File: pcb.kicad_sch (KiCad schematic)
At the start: 49 parts, among them J1 USB_B_Mini, J2 Conn_ARM_JTAG_SWD_20, J3 Micro_SD_Card_Det1, SW1 SW_RESET, U1 STM32H750VBTx, U2 USBLC6-2P6, U3 TLV1117-33, U4 W25Q128JVS, Y1 8MHz

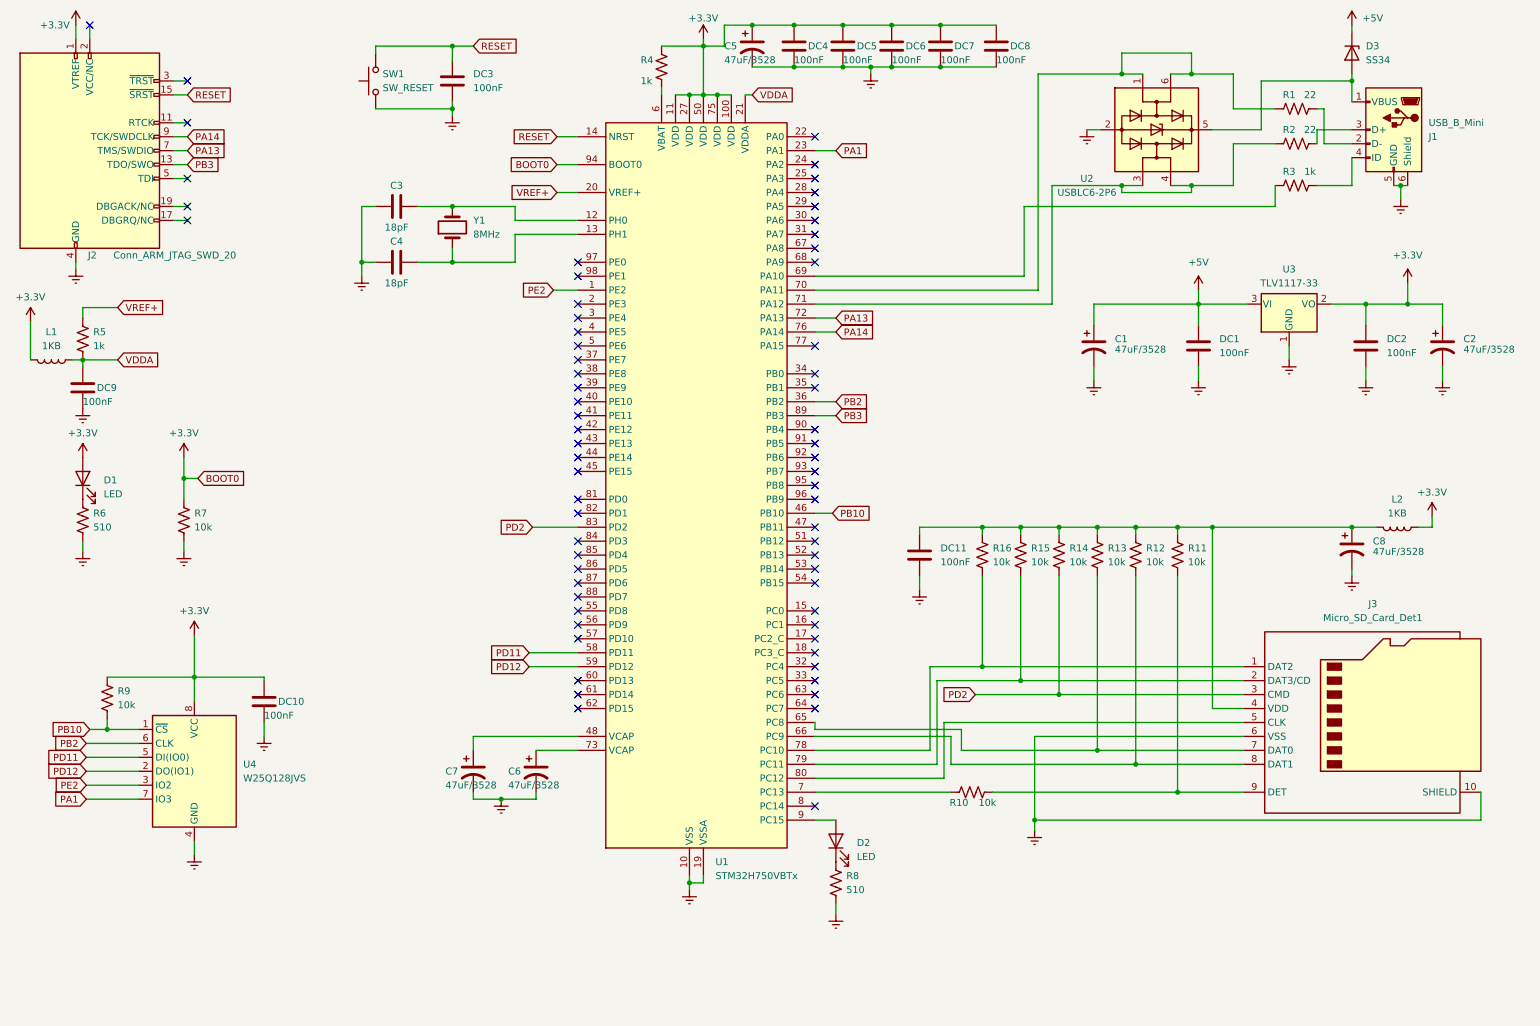
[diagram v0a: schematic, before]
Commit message: SCH: Schematic mostly finished, missing pin connectors
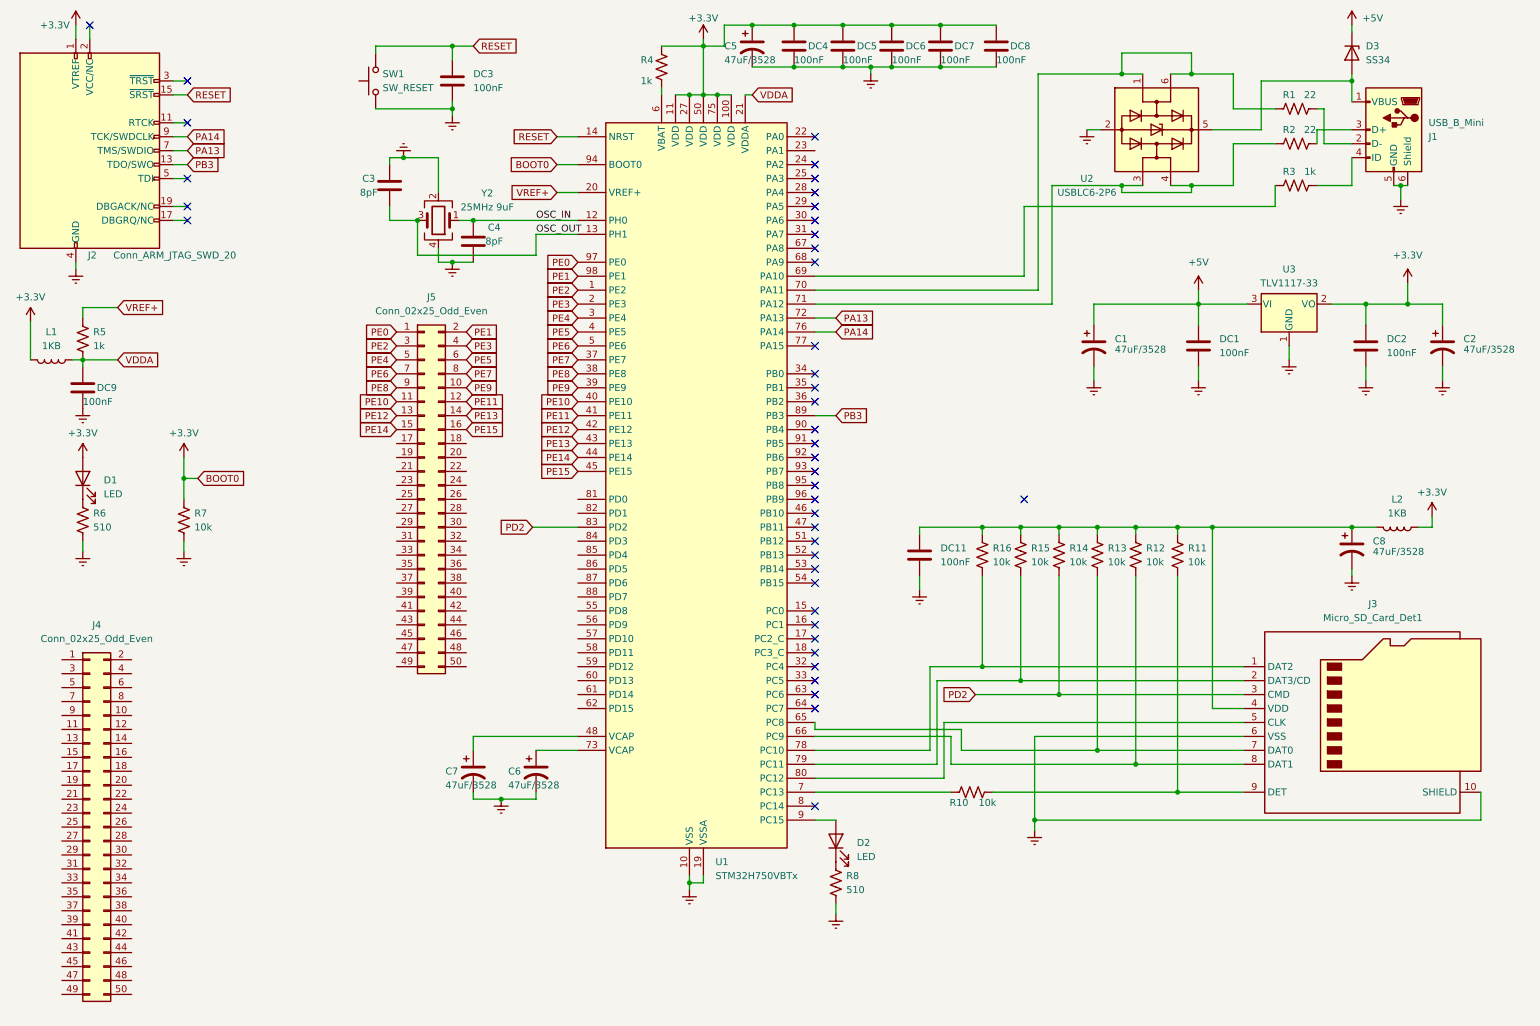
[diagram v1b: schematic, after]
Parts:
- removed DC10: 100nF, symbol Device:C
- removed R9: 10k, symbol Device:R_US
- removed U4: W25Q128JVS, Package_SO:SOIC-8_5.23x5.23mm_P1.27mm, symbol Memory_Flash:W25Q128JVS
- removed Y1: 8MHz, symbol Device:Crystal
- added J4, J5: Conn_02x25_Odd_Even, Connector_PinSocket_2.54mm:PinSocket_2x25_P2.54mm_Vertical, symbol Connector_Generic:Conn_02x25_Odd_Even
- added Y2: 25MHz 9uF, Crystal:Crystal_SMD_2016-4Pin_2.0x1.6mm, symbol Device:Crystal_GND23
- C1, C2, C5, C6, C7, C8: footprint (none) -> Capacitor_SMD:C_1206_3216Metric
- C3, C4: value 18pF -> 8pF; footprint (none) -> Capacitor_SMD:C_0402_1005Metric
- D1, D2: footprint (none) -> LED_SMD:LED_0603_1608Metric
- DC1, DC11, DC2, DC3, DC4, DC5, DC6, DC7, DC8, DC9: footprint (none) -> Capacitor_SMD:C_0402_1005Metric
- J1: footprint (none) -> Connector_USB:USB_Mini-B_Wuerth_65100516121_Horizontal
- J2: footprint (none) -> Connector_TE-Connectivity:TE_MATE-N-LOK_1-794070-x_2x10_P4.14mm_Vertical
- J3: footprint (none) -> Connector_Card:microSD_HC_Molex_104031-0811
- L1, L2: footprint (none) -> Inductor_SMD:L_0402_1005Metric
- R1, R10, R11, R12, R13, R14, R15, R16, R2, R7: footprint (none) -> Resistor_SMD:R_0402_1005Metric
- R3, R4, R5, R6, R8: footprint (none) -> Resistor_SMD:R_0603_1608Metric
- SW1: footprint (none) -> Button_Switch_SMD:SW_SPST_CK_RS282G05A3
- U3: footprint (none) -> Package_TO_SOT_SMD:SOT-223
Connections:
- net Earth: now also C4.2, Y2.2, Y2.4; no longer C4.1
- net PE2: now also J5.3 (Pin_3)
- net OSC_OUT: now reaches U1.13 (PH1)
- net OSC_OUT: now also C3.2, Y2.3; no longer C4.2
- net OSC_IN: now reaches U1.12 (PH0)
- net OSC_IN: now also C4.1, Y2.1; no longer C3.2
- net PE3: now reaches U1.2 (PE3)
- net PE3: now also J5.4 (Pin_4)
- net PE4: now reaches U1.3 (PE4)
- net PE4: now also J5.5 (Pin_5)
- net PE7: now reaches U1.37 (PE7)
- net PE7: now also J5.8 (Pin_8)
- net PE8: now reaches U1.38 (PE8)
- net PE8: now also J5.9 (Pin_9)
- net PE9: now reaches U1.39 (PE9)
- net PE9: now also J5.10 (Pin_10)
- net PE5: now reaches U1.4 (PE5)
- net PE5: now also J5.6 (Pin_6)
- net PE10: now reaches U1.40 (PE10)
- net PE10: now also J5.11 (Pin_11)
- net PE11: now reaches U1.41 (PE11)
- net PE11: now also J5.12 (Pin_12)
- net PE12: now reaches U1.42 (PE12)
- net PE12: now also J5.13 (Pin_13)
- net PE13: now reaches U1.43 (PE13)
- net PE13: now also J5.14 (Pin_14)
- net PE14: now reaches U1.44 (PE14)
- net PE14: now also J5.15 (Pin_15)
- net PE15: now reaches U1.45 (PE15)
- net PE15: now also J5.16 (Pin_16)
- net PE6: now reaches U1.5 (PE6)
- net PE6: now also J5.7 (Pin_7)
- net PE0: now reaches U1.97 (PE0)
- net PE0: now also J5.1 (Pin_1)
- net PE1: now reaches U1.98 (PE1)
- net PE1: now also J5.2 (Pin_2)
- net PA1: no longer names the net of U1.23 (PA1)
- net PB10: no longer names the net of U1.46 (PB10)
- net PB2: no longer names the net of U1.36 (PB2)
- net PD11: no longer names the net of U1.58 (PD11)
- net PD12: no longer names the net of U1.59 (PD12)
- no-connect marks 66 -> 41
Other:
- moved on the sheet: C3, C4

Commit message: ROUTE: Routing finished, still needs to be re-worked but functionality is in place
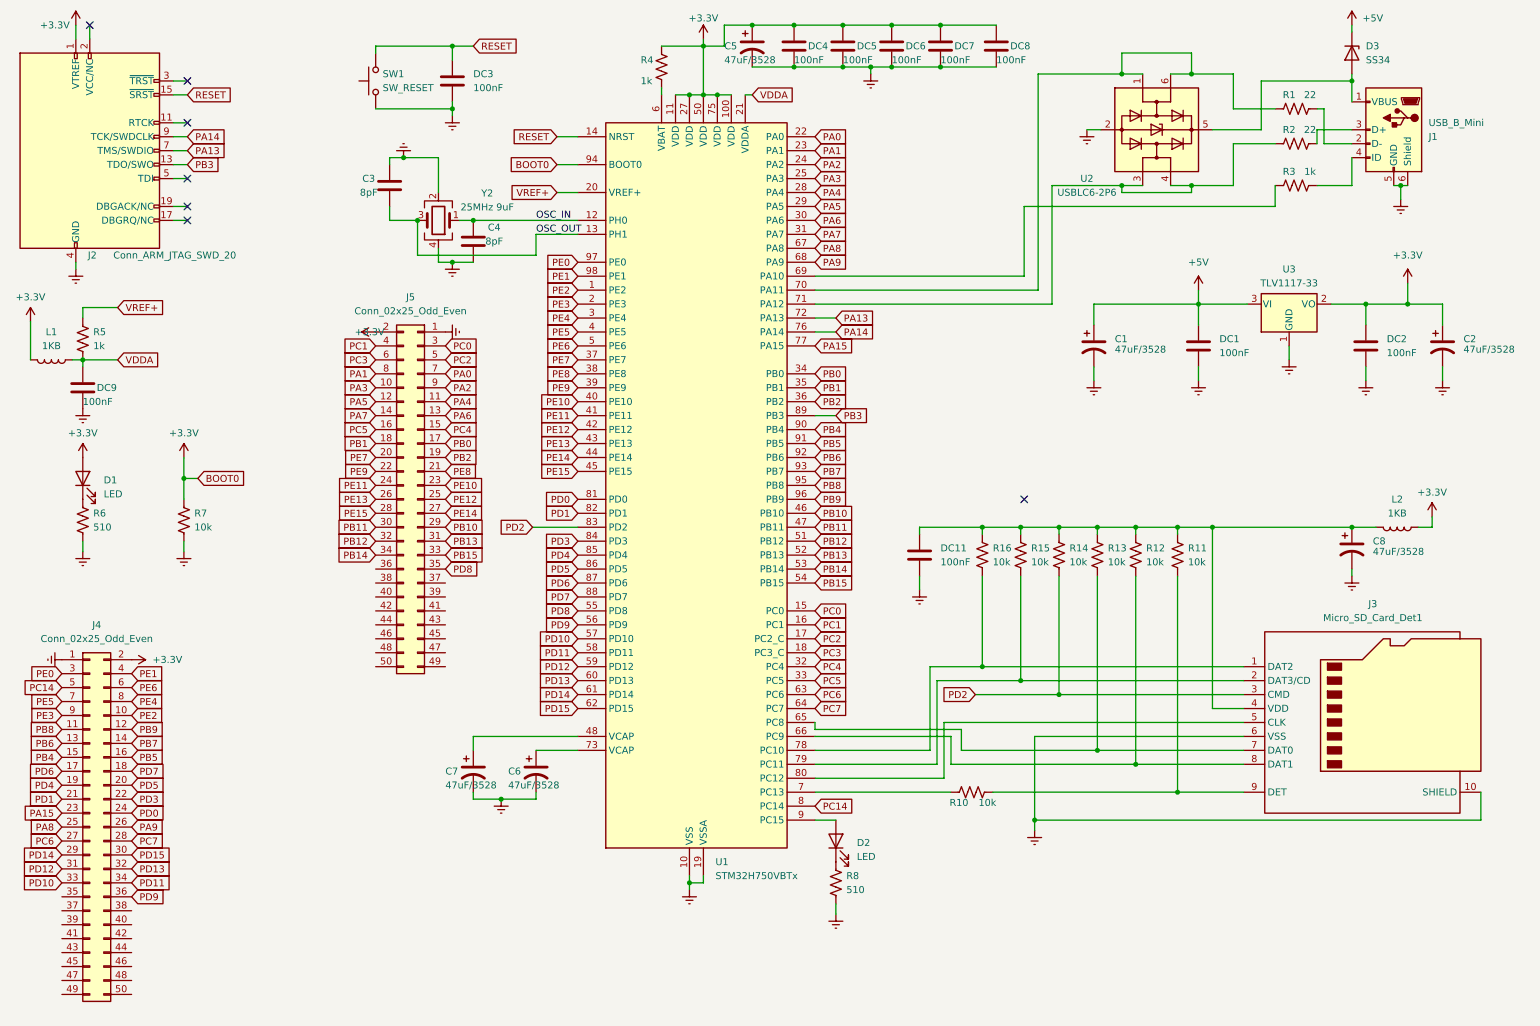
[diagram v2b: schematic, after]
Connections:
- net +3.3V: now also J4.2 (Pin_2), J5.2 (Pin_2)
- net Earth: now also J4.1 (Pin_1), J5.1 (Pin_1)
- net PE0: now also J4.3 (Pin_3); no longer J5.1 (Pin_1)
- net PE1: now also J4.4 (Pin_4); no longer J5.2 (Pin_2)
- net PE10: now also J5.23 (Pin_23); no longer J5.11 (Pin_11)
- net PE11: now also J5.24 (Pin_24); no longer J5.12 (Pin_12)
- net PE12: now also J5.25 (Pin_25); no longer J5.13 (Pin_13)
- net PE13: now also J5.26 (Pin_26); no longer J5.14 (Pin_14)
- net PE14: now also J5.27 (Pin_27); no longer J5.15 (Pin_15)
- net PE15: now also J5.28 (Pin_28); no longer J5.16 (Pin_16)
- net PE2: now also J4.10 (Pin_10); no longer J5.3 (Pin_3)
- net PE3: now also J4.9 (Pin_9); no longer J5.4 (Pin_4)
- net PE4: now also J4.8 (Pin_8); no longer J5.5 (Pin_5)
- net PE5: now also J4.7 (Pin_7); no longer J5.6 (Pin_6)
- net PE6: now also J4.6 (Pin_6); no longer J5.7 (Pin_7)
- net PE7: now also J5.20 (Pin_20); no longer J5.8 (Pin_8)
- net PE8: now also J5.21 (Pin_21); no longer J5.9 (Pin_9)
- net PE9: now also J5.22 (Pin_22); no longer J5.10 (Pin_10)
- net PB8: now reaches J4.11 (Pin_11)
- net PB8: now also U1.95 (PB8)
- net PB9: now reaches J4.12 (Pin_12)
- net PB9: now also U1.96 (PB9)
- net PB6: now reaches J4.13 (Pin_13)
- net PB6: now also U1.92 (PB6)
- net PB7: now reaches J4.14 (Pin_14)
- net PB7: now also U1.93 (PB7)
- net PB4: now reaches J4.15 (Pin_15)
- net PB4: now also U1.90 (PB4)
- net PB5: now reaches J4.16 (Pin_16)
- net PB5: now also U1.91 (PB5)
- net PD6: now reaches J4.17 (Pin_17)
- net PD6: now also U1.87 (PD6)
- net PD7: now reaches J4.18 (Pin_18)
- net PD7: now also U1.88 (PD7)
- net PD4: now reaches J4.19 (Pin_19)
- net PD4: now also U1.85 (PD4)
- net PD5: now reaches J4.20 (Pin_20)
- net PD5: now also U1.86 (PD5)
- net PD1: now reaches J4.21 (Pin_21)
- net PD1: now also U1.82 (PD1)
- net PD3: now reaches J4.22 (Pin_22)
- net PD3: now also U1.84 (PD3)
- net PA15: now reaches J4.23 (Pin_23)
- net PA15: now also U1.77 (PA15)
- net PD0: now reaches J4.24 (Pin_24)
- net PD0: now also U1.81 (PD0)
- net PA8: now reaches J4.25 (Pin_25)
- net PA8: now also U1.67 (PA8)
- net PA9: now reaches J4.26 (Pin_26)
- net PA9: now also U1.68 (PA9)
- net PC6: now reaches J4.27 (Pin_27)
- net PC6: now also U1.63 (PC6)
- net PC7: now reaches J4.28 (Pin_28)
- net PC7: now also U1.64 (PC7)
- net PD14: now reaches J4.29 (Pin_29)
- net PD14: now also U1.61 (PD14)
- net PD15: now reaches J4.30 (Pin_30)
- net PD15: now also U1.62 (PD15)
- net PD12: now reaches J4.31 (Pin_31)
- net PD12: now also U1.59 (PD12)
- net PD13: now reaches J4.32 (Pin_32)
- net PD13: now also U1.60 (PD13)
- net PD10: now reaches J4.33 (Pin_33)
- net PD10: now also U1.57 (PD10)
- net PD11: now reaches J4.34 (Pin_34)
- net PD11: now also U1.58 (PD11)
- net PD9: now reaches J4.36 (Pin_36)
- net PD9: now also U1.56 (PD9)
- net PC14: now reaches J4.5 (Pin_5)
- net PC14: now also U1.8 (PC14)
- net PB0: now reaches J5.17 (Pin_17)
- net PB0: now also U1.34 (PB0)
- net PB1: now reaches J5.18 (Pin_18)
- net PB1: now also U1.35 (PB1)
- net PB2: now reaches J5.19 (Pin_19)
- net PB2: now also U1.36 (PB2)
- net PB10: now reaches J5.29 (Pin_29)
- net PB10: now also U1.46 (PB10)
- net PB11: now reaches J5.30 (Pin_30)
- net PB11: now also U1.47 (PB11)
- net PB13: now reaches J5.31 (Pin_31)
- net PB13: now also U1.52 (PB13)
- net PB12: now reaches J5.32 (Pin_32)
- net PB12: now also U1.51 (PB12)
- net PB15: now reaches J5.33 (Pin_33)
- net PB15: now also U1.54 (PB15)
- net PB14: now reaches J5.34 (Pin_34)
- net PB14: now also U1.53 (PB14)
- net PD8: now reaches J5.35 (Pin_35)
- net PD8: now also U1.55 (PD8)
- net PC0: now reaches U1.15 (PC0)
- net PC0: now also J5.3 (Pin_3)
- net PC1: now reaches U1.16 (PC1)
- net PC1: now also J5.4 (Pin_4)
- net PC2: now reaches U1.17 (PC2_C)
- net PC2: now also J5.5 (Pin_5)
- net PC3: now reaches U1.18 (PC3_C)
- net PC3: now also J5.6 (Pin_6)
- net PA0: now reaches U1.22 (PA0)
- net PA0: now also J5.7 (Pin_7)
- net PA1: now reaches U1.23 (PA1)
- net PA1: now also J5.8 (Pin_8)
- net PA2: now reaches U1.24 (PA2)
- net PA2: now also J5.9 (Pin_9)
- net PA3: now reaches U1.25 (PA3)
- net PA3: now also J5.10 (Pin_10)
- net PA4: now reaches U1.28 (PA4)
- net PA4: now also J5.11 (Pin_11)
- net PA5: now reaches U1.29 (PA5)
- net PA5: now also J5.12 (Pin_12)
- net PA6: now reaches U1.30 (PA6)
- net PA6: now also J5.13 (Pin_13)
- net PA7: now reaches U1.31 (PA7)
- net PA7: now also J5.14 (Pin_14)
- net PC4: now reaches U1.32 (PC4)
- net PC4: now also J5.15 (Pin_15)
- net PC5: now reaches U1.33 (PC5)
- net PC5: now also J5.16 (Pin_16)
- no-connect marks 41 -> 7
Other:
- moved on the sheet: J5

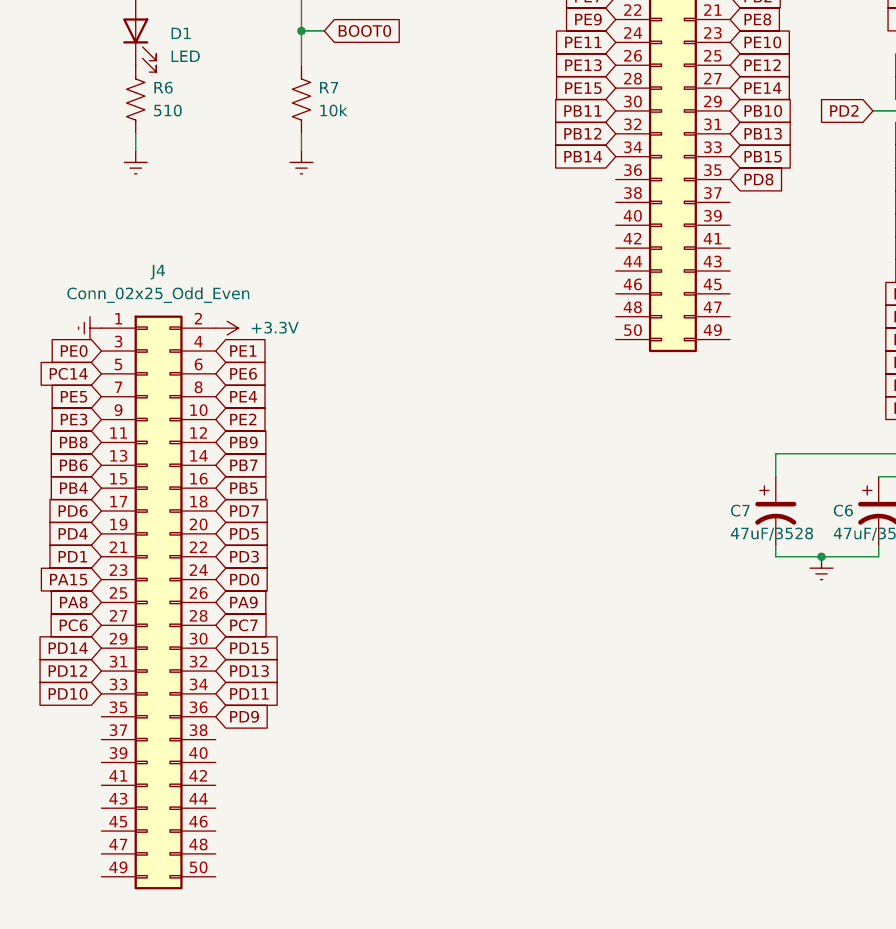
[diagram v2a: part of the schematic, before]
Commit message: PCB: Routing finished, first version
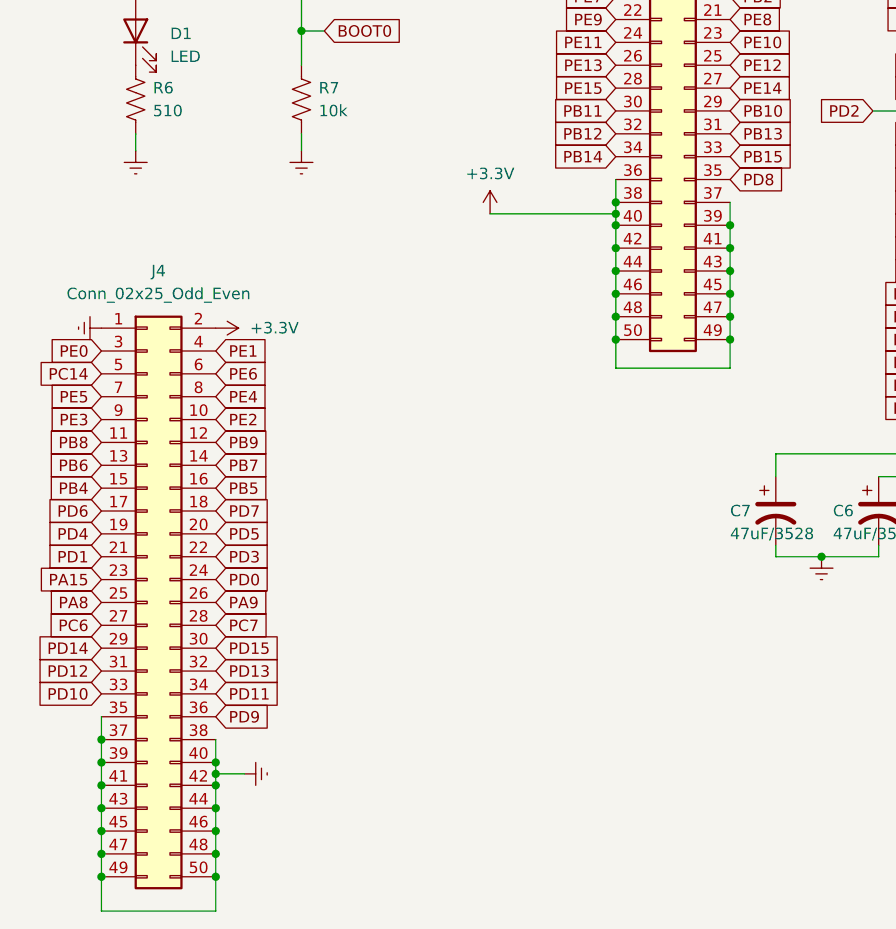
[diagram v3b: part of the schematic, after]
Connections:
- net +3.3V: now also J5.36 (Pin_36), J5.37 (Pin_37), J5.38 (Pin_38), J5.39 (Pin_39), J5.40 (Pin_40), J5.41 (Pin_41), J5.42 (Pin_42), J5.43 (Pin_43), J5.44 (Pin_44), J5.45 (Pin_45), J5.46 (Pin_46), J5.47 (Pin_47), J5.48 (Pin_48), J5.49 (Pin_49), J5.50 (Pin_50)
- net Earth: now also J4.35 (Pin_35), J4.37 (Pin_37), J4.38 (Pin_38), J4.39 (Pin_39), J4.40 (Pin_40), J4.41 (Pin_41), J4.42 (Pin_42), J4.43 (Pin_43), J4.44 (Pin_44), J4.45 (Pin_45), J4.46 (Pin_46), J4.47 (Pin_47), J4.48 (Pin_48), J4.49 (Pin_49), J4.50 (Pin_50)
